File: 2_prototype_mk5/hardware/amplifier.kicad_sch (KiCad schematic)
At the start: 8 parts, among them U1 MAX98357A

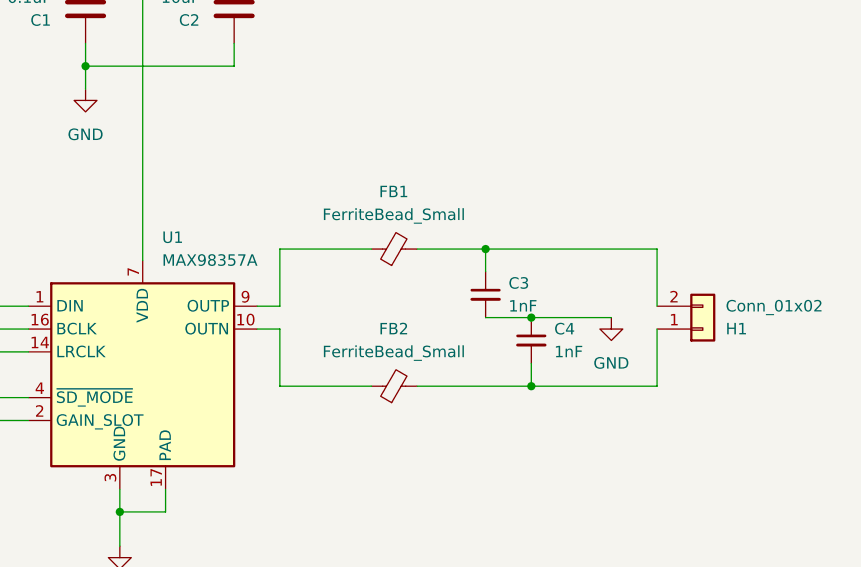
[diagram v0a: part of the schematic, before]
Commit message: Major MKV redesign using embedded RP2350
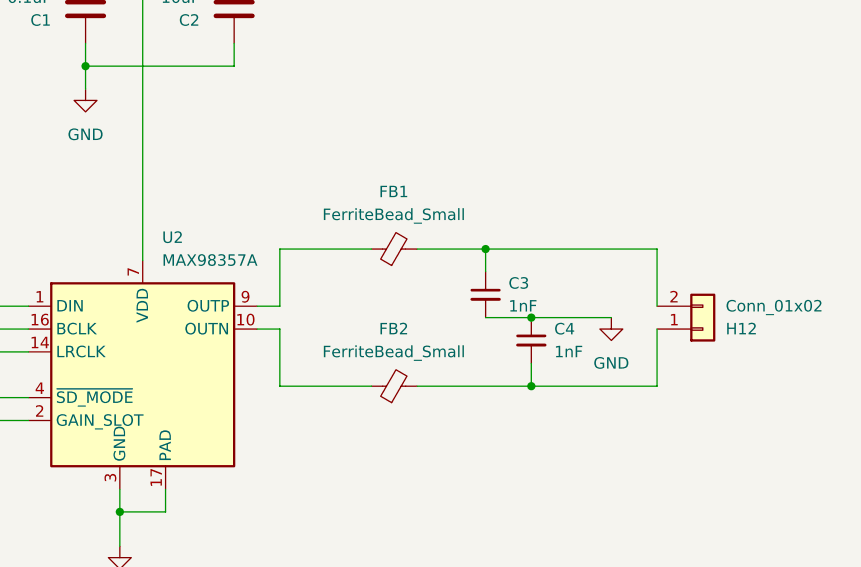
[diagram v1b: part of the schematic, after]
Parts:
- renumbered H1 to H12, U1 to U2
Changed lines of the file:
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@@
 		(in_pos_files yes)
 		(dnp no)
-		(property "Reference" "H1"
+		(property "Reference" "H12"
 			(at 214.63 100.3301 0)
 			(show_name no)
@@
 			(project "HDD Synth Prototype MK5"
 				(path "/1a22431a-ba36-40a0-9a7e-c2a82ec69c53/2950dfc3-c685-4e23-94aa-d1af22619645"
-					(reference "H1")
+					(reference "H12")
 					(unit 1)
 				)
@@
 		(in_pos_files yes)
 		(dnp no)
-		(property "Reference" "#PWR028"
+		(property "Reference" "#PWR08"
 			(at 147.32 130.81 0)
 			(hide yes)
@@
 			(project "HDD Synth Prototype MK5"
 				(path "/1a22431a-ba36-40a0-9a7e-c2a82ec69c53/2950dfc3-c685-4e23-94aa-d1af22619645"
-					(reference "#PWR028")
+					(reference "#PWR08")
 					(unit 1)
 				)
@@
 		(dnp no)
 		(fields_autoplaced yes)
-		(property "Reference" "U1"
+		(property "Reference" "U2"
 			(at 152.0033 90.17 0)
 			(show_name no)
@@
 			(project "HDD Synth Prototype MK5"
 				(path "/1a22431a-ba36-40a0-9a7e-c2a82ec69c53/2950dfc3-c685-4e23-94aa-d1af22619645"
-					(reference "U1")
+					(reference "U2")
 					(unit 1)
 				)
@@
 		(dnp no)
 		(fields_autoplaced yes)
-		(property "Reference" "#PWR034"
+		(property "Reference" "#PWR07"
 			(at 143.51 80.01 0)
 			(hide yes)
@@
 			(project "HDD Synth Prototype MK5"
 				(path "/1a22431a-ba36-40a0-9a7e-c2a82ec69c53/2950dfc3-c685-4e23-94aa-d1af22619645"
-					(reference "#PWR034")
-					(unit 1)
-				)
+					(reference "#PWR07")
+					(unit 1)
+				)

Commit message: MKV: Add LCSC numbers and resolve DRC errors
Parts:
- C1: LCSC_Part_Number (none) -> C14663
- C2: LCSC_Part_Number (none) -> C13585
- C3, C4: LCSC_Part_Number (none) -> C1588
